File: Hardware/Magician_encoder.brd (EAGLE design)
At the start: 21.6 x 39.4 mm, 24 parts, among them U1 QRE1113, U2 QRE1113

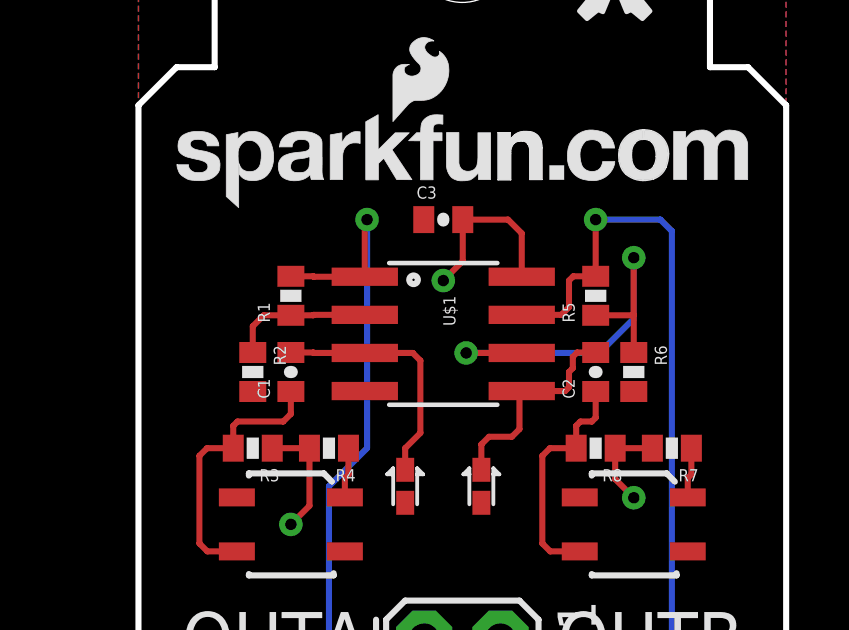
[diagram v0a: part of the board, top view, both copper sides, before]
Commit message: Changed opamp part number to U3
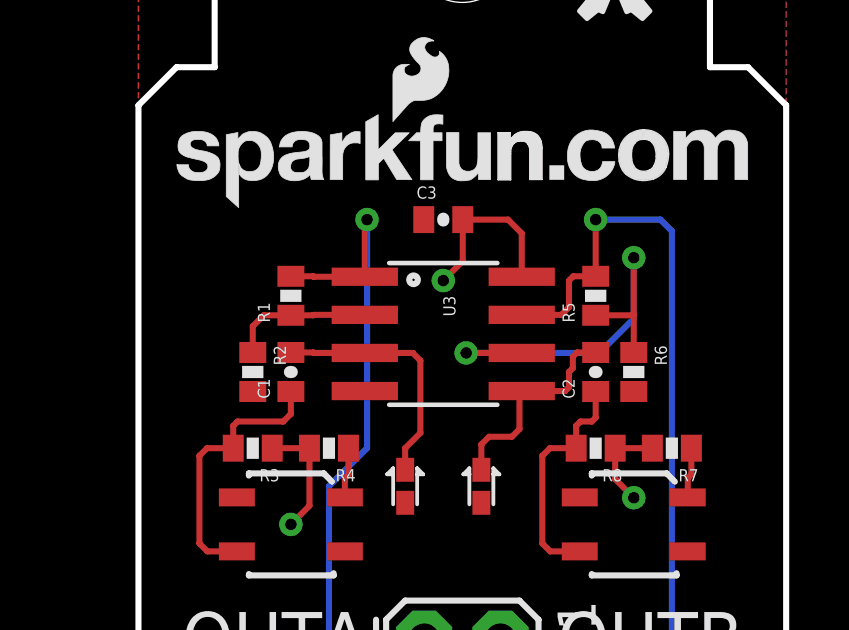
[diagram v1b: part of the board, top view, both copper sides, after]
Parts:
- renumbered U$1 to U3
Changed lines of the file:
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@@
 <grid distance="0.05" unitdist="inch" unit="inch" style="lines" multiple="1" display="yes" altdistance="0.005" altunitdist="inch" altunit="inch"/>
 <layers>
-<layer number="1" name="Top" color="4" fill="1" visible="no" active="yes"/>
+<layer number="1" name="Top" color="4" fill="1" visible="yes" active="yes"/>
 <layer number="2" name="Route2" color="1" fill="3" visible="no" active="yes"/>
 <layer number="15" name="Route15" color="4" fill="6" visible="no" active="yes"/>
@@
 <layer number="19" name="Unrouted" color="6" fill="1" visible="yes" active="yes"/>
 <layer number="20" name="Dimension" color="15" fill="1" visible="yes" active="yes"/>
-<layer number="21" name="tPlace" color="16" fill="1" visible="no" active="yes"/>
+<layer number="21" name="tPlace" color="16" fill="1" visible="yes" active="yes"/>
 <layer number="22" name="bPlace" color="14" fill="1" visible="yes" active="yes"/>
-<layer number="23" name="tOrigins" color="15" fill="1" visible="no" active="yes"/>
+<layer number="23" name="tOrigins" color="15" fill="1" visible="yes" active="yes"/>
 <layer number="24" name="bOrigins" color="15" fill="1" visible="yes" active="yes"/>
 <layer number="25" name="tNames" color="7" fill="1" visible="no" active="yes"/>
@@
 <layer number="42" name="bRestrict" color="1" fill="10" visible="no" active="yes"/>
 <layer number="44" name="Drills" color="7" fill="1" visible="no" active="yes"/>
-<layer number="45" name="Holes" color="7" fill="1" visible="no" active="yes"/>
+<layer number="45" name="Holes" color="7" fill="1" visible="yes" active="yes"/>
 <layer number="46" name="Milling" color="3" fill="1" visible="no" active="yes"/>
-<layer number="51" name="tDocu" color="6" fill="1" visible="no" active="yes"/>
+<layer number="51" name="tDocu" color="6" fill="1" visible="yes" active="yes"/>
 <layer number="52" name="bDocu" color="7" fill="1" visible="no" active="yes"/>
 <layer number="3" name="Route3" color="4" fill="3" visible="no" active="no"/>
@@
 <attribute name="PROD_ID" value="RES-07856" x="-16.51" y="-8.89" size="1.778" layer="27" rot="R270" display="off"/>
 </element>
-<element name="U$1" library="SparkFun-AnalogIC" package="SO08" value="LMV358" x="10.16" y="22.86" rot="R270">
+<element name="U3" library="SparkFun-AnalogIC" package="SO08" value="LMV358" x="10.16" y="22.86" rot="R270">
 <attribute name="PROD_ID" value="IC-09657" x="-2.54" y="-2.54" size="1.778" layer="27" rot="R270" display="off"/>
 </element>
@@
 <signals>
 <signal name="5V">
-<contactref element="U$1" pad="8"/>
+<contactref element="U3" pad="8"/>
 <contactref element="R4" pad="2"/>
 <contactref element="R3" pad="1"/>
@@
 </signal>
 <signal name="GND">
-<contactref element="U$1" pad="4"/>
+<contactref element="U3" pad="4"/>
 <contactref element="D1" pad="A"/>
 <contactref element="U2" pad="2"/>
@@
 </signal>
 <signal name="N$1">
-<contactref element="U$1" pad="2"/>
+<contactref element="U3" pad="2"/>
 <contactref element="R1" pad="1"/>
 <contactref element="R2" pad="1"/>
@@
 <signal name="OUTA">
 <contactref element="R1" pad="2"/>
-<contactref element="U$1" pad="1"/>
+<contactref element="U3" pad="1"/>
 <contactref element="JP1" pad="3"/>
 <wire x1="5.08" y1="24.78" x2="5.827" y2="24.78" width="0.2032" layer="1"/>
@@
 </signal>
 <signal name="N$6">
-<contactref element="U$1" pad="3"/>
+<contactref element="U3" pad="3"/>
 <contactref element="D1" pad="C"/>
 <contactref element="C1" pad="2"/>
@@
 <contactref element="R5" pad="1"/>
 <contactref element="R6" pad="1"/>
-<contactref element="U$1" pad="6"/>
+<contactref element="U3" pad="6"/>
 <wire x1="12.7762" y1="22.225" x2="10.922" y2="22.225" width="0.2032" layer="1"/>
 <via x="10.922" y="22.225" extent="1-16" drill="0.381"/>
@@
 <signal name="OUTB">
 <contactref element="R5" pad="2"/>
-<contactref element="U$1" pad="7"/>
+<contactref element="U3" pad="7"/>
 <contactref element="JP1" pad="4"/>
 <wire x1="12.7762" y1="23.495" x2="14.097" y2="23.495" width="0.2032" layer="1"/>
@@
 <contactref element="D2" pad="C"/>
 <contactref element="C2" pad="2"/>
-<contactref element="U$1" pad="5"/>
+<contactref element="U3" pad="5"/>
 <wire x1="11.43" y1="18.33" x2="11.43" y2="19.177" width="0.2032" layer="1"/>
 <wire x1="11.43" y1="19.177" x2="11.684" y2="19.431" width="0.2032" layer="1"/>

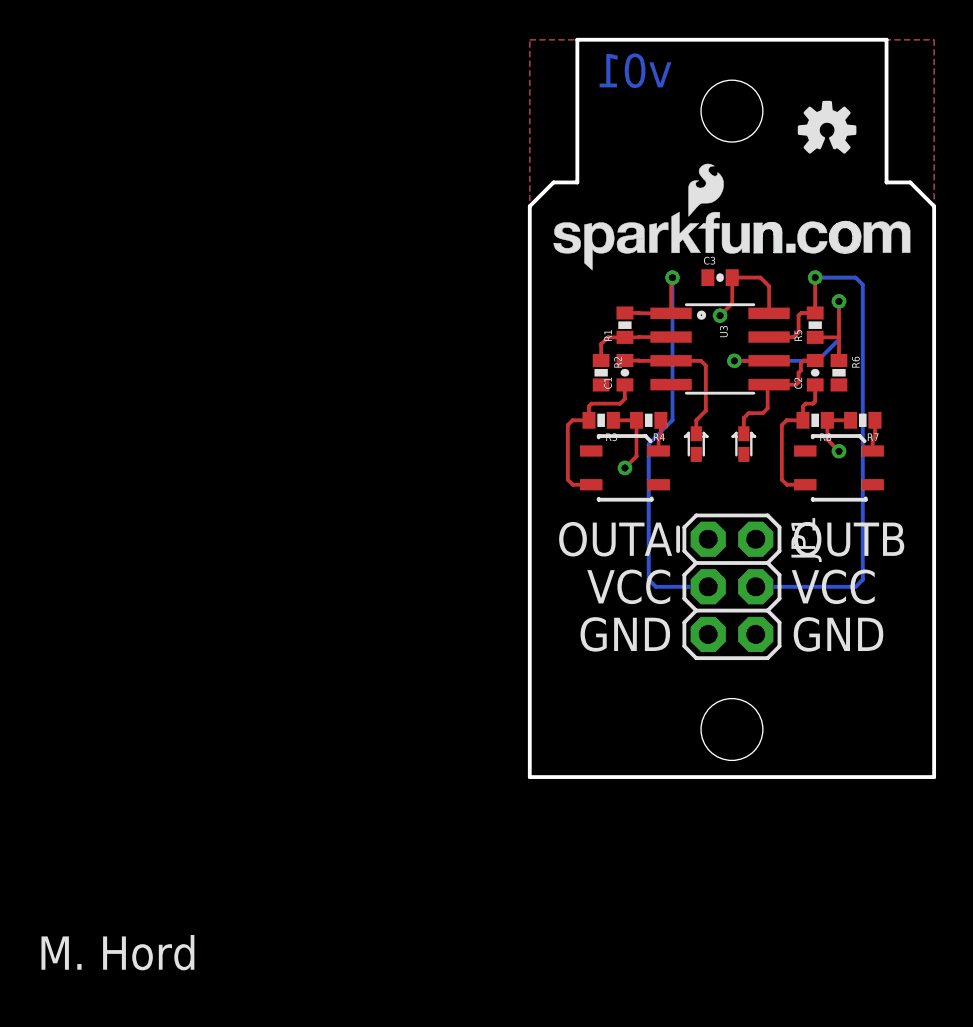
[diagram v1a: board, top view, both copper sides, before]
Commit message: Total overhaul to BJT based circuit.
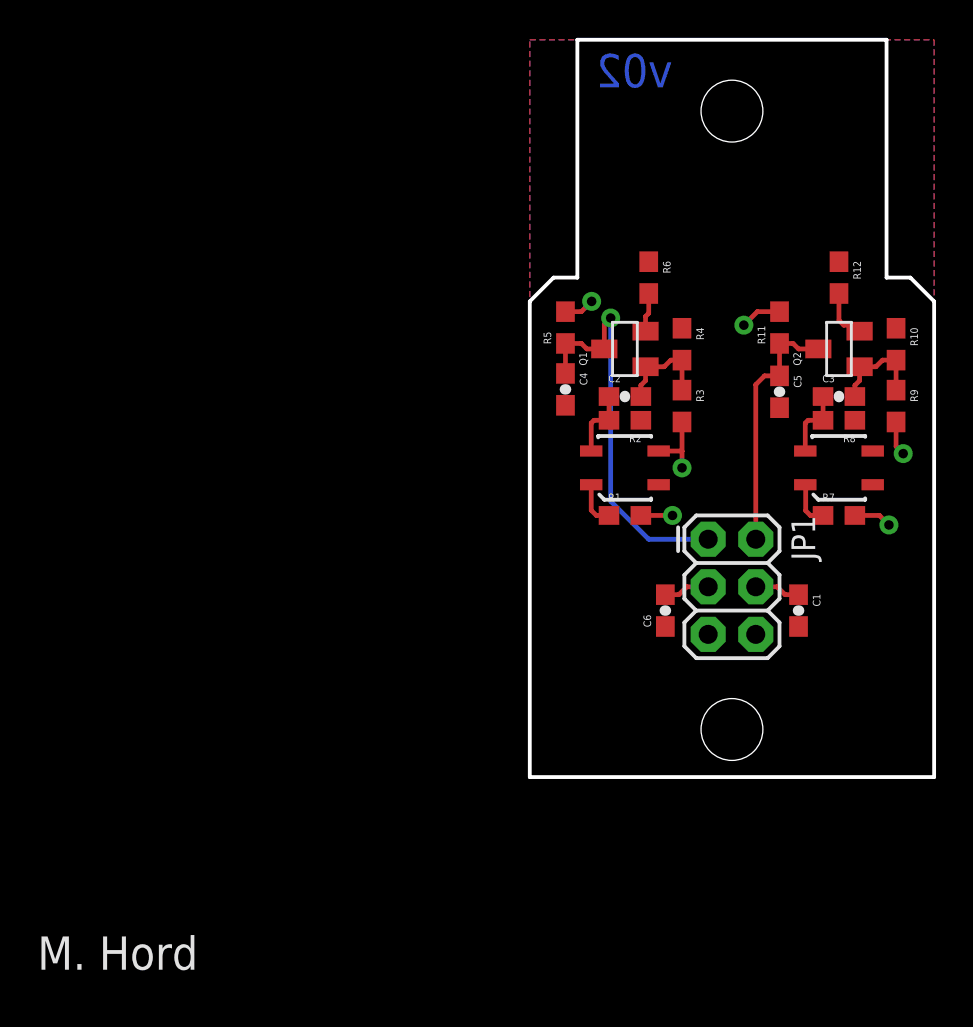
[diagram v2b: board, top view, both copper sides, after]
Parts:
- removed D1, D2: RB751, SparkFun-DiscreteSemi:SOD-523
- removed LOGO1: LOGO-SFENEW, SparkFun-Aesthetics:SFE-NEW-WEBLOGO
- removed LOGO2: OSHW-LOGOS, SparkFun-Aesthetics:OSHW-LOGO-S
- removed U3: LMV358, SparkFun-AnalogIC:SO08
- added C4, C5: 0.1uF, SparkFun-Capacitors:0603-CAP
- added C6: 1.0uF, SparkFun-Capacitors:0603-CAP
- added Q1, Q2: MMBT2222A, SparkFun-DiscreteSemi:SOT23
- added R10, R11: 10K, SparkFun-Resistors:0603
- added R12: 680, SparkFun-Resistors:0603
- added R9: 47K, SparkFun-Resistors:0603
- C1: device SparkFun-Capacitors:0402-CAP -> SparkFun-Capacitors:0603-CAP
- C2, C3: value 0.1uF -> 1.0uF; device SparkFun-Capacitors:0402-CAP -> SparkFun-Capacitors:0603-CAP
- R1: value 10k -> 100; device SparkFun-Resistors:0402-RES -> SparkFun-Resistors:0603
- R2: value 1k -> 1K; device SparkFun-Resistors:0402-RES -> SparkFun-Resistors:0603
- R3: value 10k -> 47K; device SparkFun-Resistors:0402-RES -> SparkFun-Resistors:0603
- R4: value 100 -> 10K; device SparkFun-Resistors:0402-RES -> SparkFun-Resistors:0603
- R5: value 10k -> 10K; device SparkFun-Resistors:0402-RES -> SparkFun-Resistors:0603
- R6: value 1k -> 680; device SparkFun-Resistors:0402-RES -> SparkFun-Resistors:0603
- R7: device SparkFun-Resistors:0402-RES -> SparkFun-Resistors:0603
- R8: value 10k -> 1K; device SparkFun-Resistors:0402-RES -> SparkFun-Resistors:0603
- moved C1 15.7 mm to (14.4, 8.89), turned to 270 degrees
- moved R5 13.3 mm to (1.91, 24.0)
- moved U1 11.4 mm to (5.08, 16.5), turned to 0 degrees
- moved U2 11.4 mm to (16.5, 16.5), turned to 0 degrees
- moved R6 11.4 mm to (6.35, 26.7)
- moved LOGO4 10.8 mm to (20.3, 16.3)
- moved C2 10.2 mm to (5.08, 20.3), turned to 0 degrees
- moved R1 10.2 mm to (5.08, 14.0), turned to 0 degrees
- moved C3 8.98 mm to (16.5, 20.3)
- moved R7 5.24 mm to (16.5, 14.0), turned to 0 degrees
- moved R4 4.44 mm to (8.13, 23.1), turned to 270 degrees
- moved R3 4.38 mm to (8.13, 19.8), turned to 270 degrees
- moved R2 2.84 mm to (5.08, 19.1), turned to 180 degrees
- moved R8 1.27 mm to (16.5, 19.1)
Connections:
- removed net N$11: C2.2, D2.C, U3.5
- removed net N$4: R5.1, R6.1, U3.6
- removed net N$6: C1.2, D1.C, U3.3
- new net N$2: C2.2, Q1.1, R3.1, R4.2
- new net N$7: Q2.2, R12.2
- new net N$8: C3.1, R8.2, U2.4
- net 5V: now also C1.1, C6.2, JP1.3, JP1.4, R1.2, R11.2, R3.2, R5.2, R9.2, U1.3; no longer C3.2, JP1.1, JP1.2, R3.1, R4.2, R8.1, U3.8
- net GND: now also C1.2, C4.2, C5.2, C6.1, R10.1, R12.1, R2.1, R4.1, R6.1, R8.1; no longer C3.1, D1.A, D2.A, R2.2, R6.2, U1.4, U2.4, U3.4
- net N$1: now also C2.1, R2.2, U1.4; no longer R1.1, R2.1, U3.2
- net N$10: now also U2.1; no longer U1.1
- net N$3: now also Q1.2, R6.2; no longer C1.1, R3.2, U2.3
- net N$5: now also R1.1, U1.1; no longer R4.1, U2.1
- net N$9: now also C3.2, Q2.1, R10.2, R9.1; no longer C2.1, R8.2, U1.3
- net OUTA: now also C4.1, JP1.1, Q1.3, R5.1; no longer JP1.3, R1.2, U3.1
- net OUTB: now also C5.1, JP1.2, Q2.3, R11.1; no longer JP1.4, R5.2, U3.7
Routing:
- net OUTB: track 29.7 -> 13.6 mm, vias 1 -> 0
- net N$4: track 14.4 -> 0.00 mm, vias 2 -> 0
- net N$6: track 8.28 -> 0.00 mm
- net N$11: track 7.15 -> 0.00 mm
- net N$3: track 9.09 -> 2.08 mm
- net N$2: track 0.00 -> 5.39 mm
- net 5V: track 13.1 -> 18.0 mm, vias 3 -> 6
- net N$8: track 0.00 -> 3.77 mm
- net N$7: track 0.00 -> 3.20 mm
- net OUTA: track 24.4 -> 21.4 mm
- net N$9: track 7.89 -> 5.39 mm
- net N$1: track 4.77 -> 3.77 mm
- net N$5: track 1.69 -> 2.43 mm
- net N$10: track 1.69 -> 2.43 mm
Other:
- outline, holes or cut-outs redrawn
- board text added: "v02"
- board text removed: "v01"

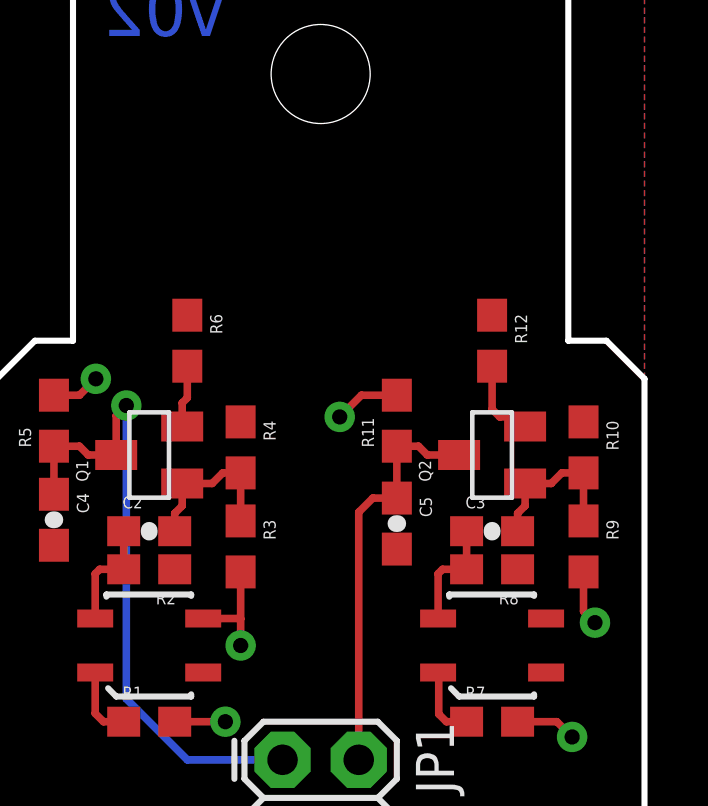
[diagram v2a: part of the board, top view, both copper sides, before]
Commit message: Change to discrete BJT circuit.
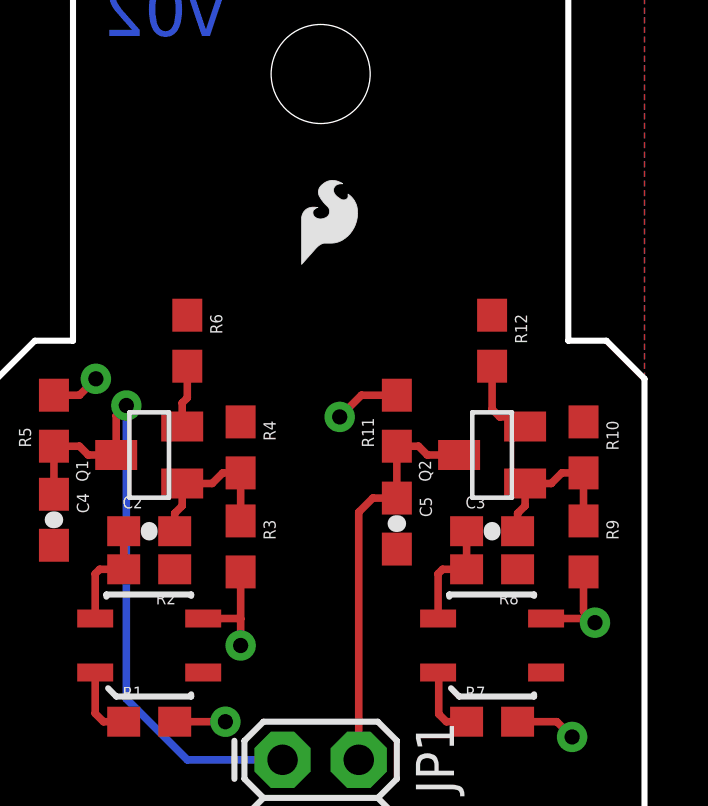
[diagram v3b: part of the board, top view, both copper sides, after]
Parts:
- added LOGO1: LOGO-SFESK, SparkFun-Aesthetics:SFE-LOGO-FLAME
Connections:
- net 5V: now also U2.3
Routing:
- net 5V: track 18.0 -> 19.7 mm
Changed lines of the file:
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@@
 <grid distance="0.05" unitdist="inch" unit="inch" style="lines" multiple="1" display="yes" altdistance="0.005" altunitdist="inch" altunit="inch"/>
 <layers>
-<layer number="1" name="Top" color="4" fill="1" visible="no" active="yes"/>
+<layer number="1" name="Top" color="4" fill="1" visible="yes" active="yes"/>
 <layer number="2" name="Route2" color="1" fill="3" visible="no" active="yes"/>
 <layer number="15" name="Route15" color="4" fill="6" visible="no" active="yes"/>
@@
 <layer number="19" name="Unrouted" color="6" fill="1" visible="yes" active="yes"/>
 <layer number="20" name="Dimension" color="15" fill="1" visible="yes" active="yes"/>
-<layer number="21" name="tPlace" color="16" fill="1" visible="no" active="yes"/>
+<layer number="21" name="tPlace" color="16" fill="1" visible="yes" active="yes"/>
 <layer number="22" name="bPlace" color="14" fill="1" visible="yes" active="yes"/>
-<layer number="23" name="tOrigins" color="15" fill="1" visible="no" active="yes"/>
+<layer number="23" name="tOrigins" color="15" fill="1" visible="yes" active="yes"/>
 <layer number="24" name="bOrigins" color="15" fill="1" visible="yes" active="yes"/>
 <layer number="25" name="tNames" color="7" fill="1" visible="no" active="yes"/>
@@
 <layer number="42" name="bRestrict" color="1" fill="10" visible="no" active="yes"/>
 <layer number="44" name="Drills" color="7" fill="1" visible="no" active="yes"/>
-<layer number="45" name="Holes" color="7" fill="1" visible="no" active="yes"/>
+<layer number="45" name="Holes" color="7" fill="1" visible="yes" active="yes"/>
 <layer number="46" name="Milling" color="3" fill="1" visible="no" active="yes"/>
-<layer number="51" name="tDocu" color="6" fill="1" visible="no" active="yes"/>
+<layer number="51" name="tDocu" color="6" fill="1" visible="yes" active="yes"/>
 <layer number="52" name="bDocu" color="7" fill="1" visible="no" active="yes"/>
 <layer number="3" name="Route3" color="4" fill="3" visible="no" active="no"/>
@@
 <attribute name="PROD_ID" value="TRANS-08049" x="16.51" y="22.86" size="1.778" layer="27" font="vector" ratio="15" rot="R90" display="off"/>
 </element>
+<element name="LOGO1" library="SparkFun-Aesthetics" package="SFE-LOGO-FLAME" value="LOGO-SFESK" x="10.16" y="29.21"/>
 </elements>
 <signals>
@@
 <wire x1="13.628" y1="9.74" x2="13.208" y2="10.16" width="0.254" layer="1"/>
 <wire x1="13.208" y1="10.16" x2="12.065" y2="10.16" width="0.254" layer="1"/>
+<contactref element="U2" pad="3"/>
+<wire x1="18.31" y1="17.41" x2="19.801" y2="17.41" width="0.254" layer="1"/>
+<wire x1="19.801" y1="17.41" x2="19.939" y2="17.272" width="0.254" layer="1"/>
 </signal>
 <signal name="GND">
